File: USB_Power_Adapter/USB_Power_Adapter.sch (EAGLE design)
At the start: 6 parts

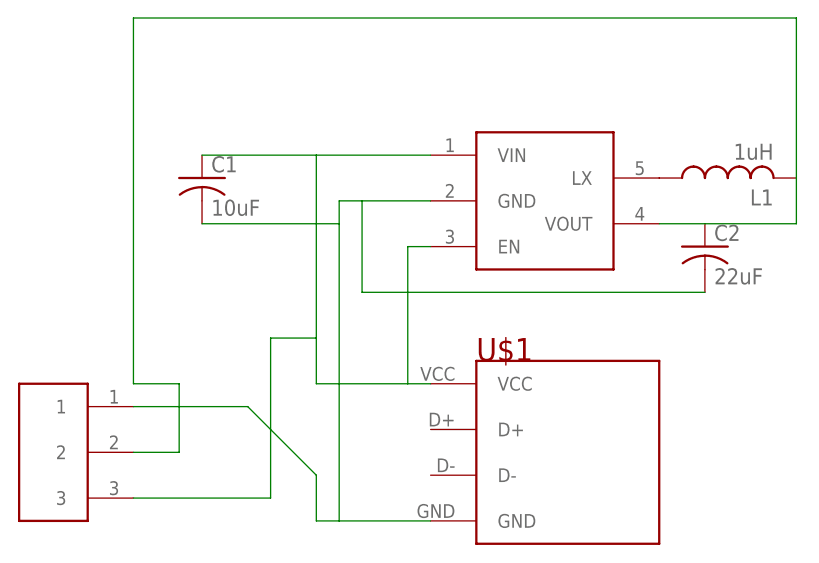
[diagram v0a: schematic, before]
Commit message: Forced name U1
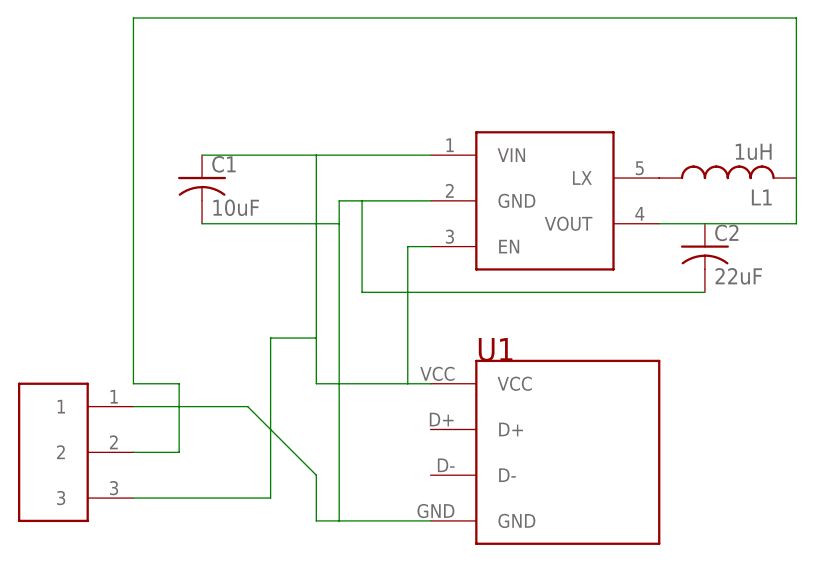
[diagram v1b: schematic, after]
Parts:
- renumbered U$1 to U1
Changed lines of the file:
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@@
 </classes>
 <parts>
-<part name="U$1" library="ScottSilver" deviceset="MICROUSB" device="MICROUSB_THRU"/>
+<part name="U1" library="ScottSilver" deviceset="MICROUSB" device="MICROUSB_THRU"/>
 <part name="U$3" library="ScottSilver" deviceset="SC189" device=""/>
 <part name="C1" library="resistor" deviceset="C-US" device="C0805K" value="10uF"/>
@@
 </plain>
 <instances>
-<instance part="U$1" gate="G$1" x="60.96" y="55.88"/>
+<instance part="U1" gate="G$1" x="60.96" y="55.88"/>
 <instance part="U$3" gate="G$1" x="58.42" y="83.82"/>
 <instance part="C1" gate="G$1" x="20.32" y="86.36"/>
@@
 <net name="N$1" class="0">
 <segment>
-<pinref part="U$1" gate="G$1" pin="VCC"/>
+<pinref part="U1" gate="G$1" pin="VCC"/>
 <wire x1="33.02" y1="63.5" x2="43.18" y2="63.5" width="0.1524" layer="91"/>
 <wire x1="43.18" y1="63.5" x2="45.72" y2="63.5" width="0.1524" layer="91"/>
@@
 <net name="GND" class="0">
 <segment>
-<pinref part="U$1" gate="G$1" pin="GND"/>
+<pinref part="U1" gate="G$1" pin="GND"/>
 <wire x1="33.02" y1="53.34" x2="33.02" y2="48.26" width="0.1524" layer="91"/>
 <wire x1="33.02" y1="48.26" x2="35.56" y2="48.26" width="0.1524" layer="91"/>

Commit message: Fixed junctions
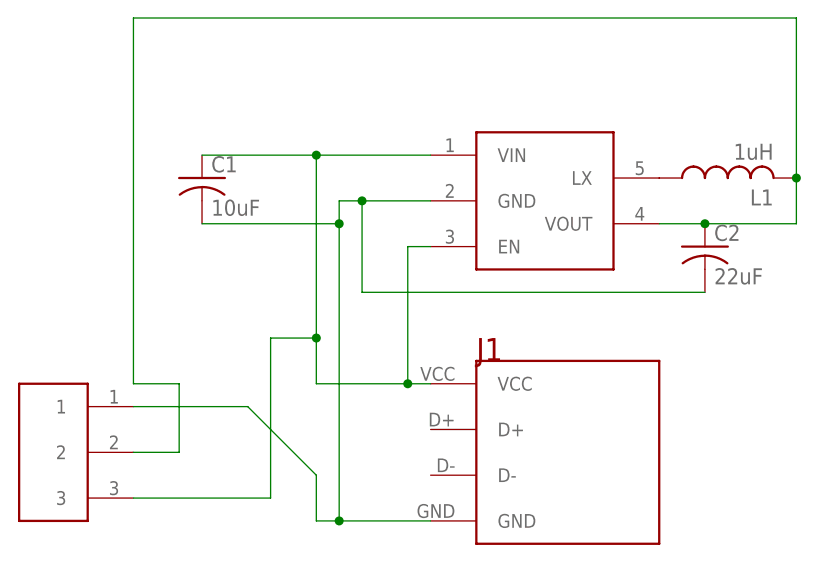
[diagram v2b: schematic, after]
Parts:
- removed U$3: SC189, ScottSilver:SC189
- added J1: MICROUSBMICROUSB_THRU, ScottSilver:MICROUSBMICROUSB_THRU
- U1: value MICROUSBMICROUSB_THRU -> SC189; device ScottSilver:MICROUSBMICROUSB_THRU -> ScottSilver:SC189
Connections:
- net GND: now also J1.GND; no longer U$3.GND
- net LX: now also U1.LX; no longer U$3.LX
- net N$1: now also J1.VCC, U1.EN, U1.VIN; no longer U$3.EN, U$3.VIN, U1.VCC
- net N$3: now also U1.VOUT; no longer U$3.VOUT
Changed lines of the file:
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@@
 </classes>
 <parts>
-<part name="U1" library="ScottSilver" deviceset="MICROUSB" device="MICROUSB_THRU"/>
-<part name="U$3" library="ScottSilver" deviceset="SC189" device=""/>
+<part name="J1" library="ScottSilver" deviceset="MICROUSB" device="MICROUSB_THRU"/>
+<part name="U1" library="ScottSilver" deviceset="SC189" device=""/>
 <part name="C1" library="resistor" deviceset="C-US" device="C0805K" value="10uF"/>
 <part name="C2" library="resistor" deviceset="C-US" device="C0805K" value="22uF"/>
@@
 </plain>
 <instances>
-<instance part="U1" gate="G$1" x="60.96" y="55.88"/>
-<instance part="U$3" gate="G$1" x="58.42" y="83.82"/>
+<instance part="J1" gate="G$1" x="60.96" y="55.88"/>
+<instance part="U1" gate="G$1" x="58.42" y="83.82"/>
 <instance part="C1" gate="G$1" x="20.32" y="86.36"/>
 <instance part="C2" gate="G$1" x="76.2" y="78.74"/>
@@
 <net name="N$1" class="0">
 <segment>
-<pinref part="U1" gate="G$1" pin="VCC"/>
+<pinref part="J1" gate="G$1" pin="VCC"/>
 <wire x1="33.02" y1="63.5" x2="43.18" y2="63.5" width="0.1524" layer="91"/>
 <wire x1="43.18" y1="63.5" x2="45.72" y2="63.5" width="0.1524" layer="91"/>
 <wire x1="33.02" y1="63.5" x2="33.02" y2="68.58" width="0.1524" layer="91"/>
-<pinref part="U$3" gate="G$1" pin="VIN"/>
+<pinref part="U1" gate="G$1" pin="VIN"/>
 <wire x1="33.02" y1="68.58" x2="33.02" y2="88.9" width="0.1524" layer="91"/>
 <wire x1="33.02" y1="88.9" x2="45.72" y2="88.9" width="0.1524" layer="91"/>
-<pinref part="U$3" gate="G$1" pin="EN"/>
+<pinref part="U1" gate="G$1" pin="EN"/>
 <wire x1="45.72" y1="78.74" x2="43.18" y2="78.74" width="0.1524" layer="91"/>
 <wire x1="43.18" y1="78.74" x2="43.18" y2="63.5" width="0.1524" layer="91"/>
@@
 <wire x1="27.94" y1="68.58" x2="33.02" y2="68.58" width="0.1524" layer="91"/>
 <pinref part="U$2" gate="G$1" pin="3"/>
+<junction x="33.02" y="88.9"/>
+<junction x="33.02" y="68.58"/>
+<junction x="43.18" y="63.5"/>
 </segment>
 </net>
 <net name="GND" class="0">
 <segment>
-<pinref part="U1" gate="G$1" pin="GND"/>
+<pinref part="J1" gate="G$1" pin="GND"/>
 <wire x1="33.02" y1="53.34" x2="33.02" y2="48.26" width="0.1524" layer="91"/>
 <wire x1="33.02" y1="48.26" x2="35.56" y2="48.26" width="0.1524" layer="91"/>
 <wire x1="35.56" y1="48.26" x2="45.72" y2="48.26" width="0.1524" layer="91"/>
 <wire x1="35.56" y1="48.26" x2="35.56" y2="81.28" width="0.1524" layer="91"/>
-<pinref part="U$3" gate="G$1" pin="GND"/>
+<pinref part="U1" gate="G$1" pin="GND"/>
 <wire x1="35.56" y1="81.28" x2="35.56" y2="83.82" width="0.1524" layer="91"/>
 <wire x1="35.56" y1="83.82" x2="38.1" y2="83.82" width="0.1524" layer="91"/>
@@
 <wire x1="25.4" y1="60.96" x2="33.02" y2="53.34" width="0.1524" layer="91"/>
 <pinref part="U$2" gate="G$1" pin="1"/>
+<junction x="35.56" y="81.28"/>
+<junction x="38.1" y="83.82"/>
+<junction x="35.56" y="48.26"/>
 </segment>
 </net>
 <net name="N$3" class="0">
 <segment>
-<pinref part="U$3" gate="G$1" pin="VOUT"/>
+<pinref part="U1" gate="G$1" pin="VOUT"/>
 <pinref part="C2" gate="G$1" pin="1"/>
 <wire x1="71.12" y1="81.28" x2="76.2" y2="81.28" width="0.1524" layer="91"/>
@@
 <wire x1="17.78" y1="55.88" x2="17.78" y2="63.5" width="0.1524" layer="91"/>
 <pinref part="U$2" gate="G$1" pin="2"/>
+<junction x="76.2" y="81.28"/>
+<junction x="86.36" y="86.36"/>
 </segment>
 </net>
 <net name="LX" class="0">
 <segment>
-<pinref part="U$3" gate="G$1" pin="LX"/>
+<pinref part="U1" gate="G$1" pin="LX"/>
 <pinref part="L1" gate="G$1" pin="1"/>
 </segment>
